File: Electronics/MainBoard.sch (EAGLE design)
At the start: 10 parts, among them J1 1X2-3.5MM

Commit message: nearly done
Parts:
- added R1, R2: (no value), fab:RES-US1206
- added U$1: USB-MINIB-5PIN, SparkFun:USB-MINIB-5PIN
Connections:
- removed net A16: JP1.16
- removed net G_ENC_A_2: JP5.7
- removed net G_ENC_B_2: JP5.8
- removed net P12: JP1.12
- removed net P21: JP2.1
- removed net P22: JP2.2
- removed net P23: JP2.3
- removed net P24: JP2.4
- removed net P25: JP2.5
- removed net P26: JP2.6
- removed net P29: JP2.9
- removed net P30: JP2.10
- new net A_20: JP1.20
- new net D+: JP2.11, R2.1, U$1.D+
- new net D-: JP2.12, R1.1, U$1.D-
- new net G_ENCA_2: JP2.3, JP5.7
- new net G_ENCB_2: JP2.4, JP5.8
- new net P5: JP1.5
- net GND: now also R1.2, R2.2, U$1.GND
- net G_CS_2: now also JP1.16; no longer JP1.20
- net G_DIR_2: now also JP1.12
- net G_PWM_1: now also JP2.2; no longer JP1.5
- net G_PWM_2: now also JP2.1
- net MOT_DIR: now also JP2.5
- net MOT_ENC_A: now also JP2.10
- net MOT_ENC_B: now also JP2.9
- net MOT_PWM: now also JP2.6
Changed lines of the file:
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@@
 <part name="8V1" library="SparkFun" deviceset="VCC" device="" value="8V"/>
 <part name="8V2" library="SparkFun" deviceset="VCC" device="" value="8V"/>
+<part name="R1" library="fab" deviceset="RES-US" device="1206"/>
+<part name="R2" library="fab" deviceset="RES-US" device="1206"/>
+<part name="GND2" library="SparkFun" deviceset="GND" device=""/>
+<part name="U$1" library="SparkFun" deviceset="USB-MINIB" device="-5PIN"/>
+<part name="GND3" library="SparkFun" deviceset="GND" device=""/>
 </parts>
 <sheets>
@@
 <instance part="8V1" gate="1" x="78.74" y="193.04"/>
 <instance part="8V2" gate="1" x="45.72" y="170.18"/>
+<instance part="R1" gate="G$1" x="81.28" y="88.9"/>
+<instance part="R2" gate="G$1" x="81.28" y="83.82"/>
+<instance part="GND2" gate="1" x="91.44" y="78.74"/>
+<instance part="U$1" gate="G$1" x="-15.24" y="137.16"/>
+<instance part="GND3" gate="1" x="-30.48" y="132.08"/>
 </instances>
 <busses>
@@
 <wire x1="-20.32" y1="193.04" x2="-22.86" y2="193.04" width="0.1524" layer="91"/>
 </segment>
+<segment>
+<pinref part="R2" gate="G$1" pin="2"/>
+<wire x1="86.36" y1="83.82" x2="91.44" y2="83.82" width="0.1524" layer="91"/>
+<wire x1="91.44" y1="83.82" x2="91.44" y2="88.9" width="0.1524" layer="91"/>
+<pinref part="R1" gate="G$1" pin="2"/>
+<wire x1="91.44" y1="88.9" x2="86.36" y2="88.9" width="0.1524" layer="91"/>
+<pinref part="GND2" gate="1" pin="GND"/>
+<wire x1="91.44" y1="83.82" x2="91.44" y2="81.28" width="0.1524" layer="91"/>
+<junction x="91.44" y="83.82"/>
+</segment>
+<segment>
+<pinref part="U$1" gate="G$1" pin="GND"/>
+<wire x1="-17.78" y1="137.16" x2="-30.48" y2="137.16" width="0.1524" layer="91"/>
+<pinref part="GND3" gate="1" pin="GND"/>
+<wire x1="-30.48" y1="137.16" x2="-30.48" y2="134.62" width="0.1524" layer="91"/>
+</segment>
 </net>
 <net name="5V" class="0">
@@
 </segment>
 </net>
-<net name="P30" class="0">
-<segment>
-<pinref part="JP2" gate="A" pin="10"/>
-<wire x1="45.72" y1="81.28" x2="73.66" y2="81.28" width="0.1524" layer="91"/>
-<label x="53.34" y="81.28" size="1.778" layer="95"/>
-</segment>
-</net>
-<net name="P29" class="0">
-<segment>
-<pinref part="JP2" gate="A" pin="9"/>
-<wire x1="45.72" y1="78.74" x2="73.66" y2="78.74" width="0.1524" layer="91"/>
-<label x="53.34" y="78.74" size="1.778" layer="95"/>
-</segment>
-</net>
-<net name="P26" class="0">
-<segment>
-<pinref part="JP2" gate="A" pin="6"/>
-<wire x1="45.72" y1="71.12" x2="73.66" y2="71.12" width="0.1524" layer="91"/>
-<label x="53.34" y="71.12" size="1.778" layer="95"/>
-</segment>
-</net>
-<net name="P25" class="0">
-<segment>
-<pinref part="JP2" gate="A" pin="5"/>
-<wire x1="45.72" y1="68.58" x2="73.66" y2="68.58" width="0.1524" layer="91"/>
-<label x="53.34" y="68.58" size="1.778" layer="95"/>
-</segment>
-</net>
-<net name="P24" class="0">
+<net name="G_ENCB_2" class="0">
 <segment>
 <pinref part="JP2" gate="A" pin="4"/>
@@
 <label x="53.34" y="66.04" size="1.778" layer="95"/>
 </segment>
-</net>
-<net name="P22" class="0">
-<segment>
-<pinref part="JP2" gate="A" pin="2"/>
-<wire x1="45.72" y1="60.96" x2="73.66" y2="60.96" width="0.1524" layer="91"/>
-<label x="53.34" y="60.96" size="1.778" layer="95"/>
-</segment>
-</net>
-<net name="P21" class="0">
-<segment>
-<pinref part="JP2" gate="A" pin="1"/>
-<wire x1="45.72" y1="58.42" x2="73.66" y2="58.42" width="0.1524" layer="91"/>
-<label x="53.34" y="58.42" size="1.778" layer="95"/>
-</segment>
-</net>
-<net name="P12" class="0">
-<segment>
-<pinref part="JP1" gate="A" pin="12"/>
-<wire x1="15.24" y1="78.74" x2="-7.62" y2="78.74" width="0.1524" layer="91"/>
-<label x="-7.62" y="78.74" size="1.778" layer="95"/>
+<segment>
+<pinref part="JP5" gate="G$1" pin="8"/>
+<wire x1="68.58" y1="147.32" x2="48.26" y2="147.32" width="0.1524" layer="91"/>
+<label x="48.26" y="147.32" size="1.778" layer="95"/>
 </segment>
 </net>
@@
 <wire x1="15.24" y1="73.66" x2="-7.62" y2="73.66" width="0.1524" layer="91"/>
 <label x="-7.62" y="73.66" size="1.778" layer="95"/>
-</segment>
-</net>
-<net name="A16" class="0">
-<segment>
-<pinref part="JP1" gate="A" pin="16"/>
-<wire x1="15.24" y1="68.58" x2="-7.62" y2="68.58" width="0.1524" layer="91"/>
-<label x="-7.62" y="68.58" size="1.778" layer="95"/>
 </segment>
 </net>
@@
 </segment>
 </net>
-<net name="P23" class="0">
+<net name="G_ENCA_2" class="0">
 <segment>
 <pinref part="JP2" gate="A" pin="3"/>
 <wire x1="45.72" y1="63.5" x2="73.66" y2="63.5" width="0.1524" layer="91"/>
 <label x="53.34" y="63.5" size="1.778" layer="95"/>
+</segment>
+<segment>
+<pinref part="JP5" gate="G$1" pin="7"/>
+<wire x1="68.58" y1="149.86" x2="48.26" y2="149.86" width="0.1524" layer="91"/>
+<label x="48.26" y="149.86" size="1.778" layer="95"/>
 </segment>
 </net>
@@
 </segment>
 <segment>
-<pinref part="JP1" gate="A" pin="5"/>
-<wire x1="15.24" y1="96.52" x2="-7.62" y2="96.52" width="0.1524" layer="91"/>
-<label x="-7.62" y="96.52" size="1.778" layer="95"/>
+<pinref part="JP2" gate="A" pin="2"/>
+<wire x1="45.72" y1="60.96" x2="73.66" y2="60.96" width="0.1524" layer="91"/>
+<label x="53.34" y="60.96" size="1.778" layer="95"/>
 </segment>
 </net>
@@
 <label x="48.26" y="154.94" size="1.778" layer="95"/>
 </segment>
+<segment>
+<pinref part="JP2" gate="A" pin="1"/>
+<wire x1="45.72" y1="58.42" x2="73.66" y2="58.42" width="0.1524" layer="91"/>
+<label x="53.34" y="58.42" size="1.778" layer="95"/>
+</segment>
 </net>
 <net name="G_DIR_2" class="0">
@@
 <label x="48.26" y="152.4" size="1.778" layer="95"/>
 </segment>
-</net>
-<net name="G_ENC_A_2" class="0">
-<segment>
-<pinref part="JP5" gate="G$1" pin="7"/>
-<wire x1="68.58" y1="149.86" x2="48.26" y2="149.86" width="0.1524" layer="91"/>
-<label x="48.26" y="149.86" size="1.778" layer="95"/>
-</segment>
-</net>
-<net name="G_ENC_B_2" class="0">
-<segment>
-<pinref part="JP5" gate="G$1" pin="8"/>
-<wire x1="68.58" y1="147.32" x2="48.26" y2="147.32" width="0.1524" layer="91"/>
-<label x="48.26" y="147.32" size="1.778" layer="95"/>
+<segment>
+<pinref part="JP1" gate="A" pin="12"/>
+<wire x1="15.24" y1="78.74" x2="-7.62" y2="78.74" width="0.1524" layer="91"/>
+<label x="-7.62" y="78.74" size="1.778" layer="95"/>
 </segment>
 </net>
@@
 <label x="17.78" y="149.86" size="1.778" layer="95"/>
 </segment>
+<segment>
+<pinref part="JP2" gate="A" pin="9"/>
+<wire x1="45.72" y1="78.74" x2="73.66" y2="78.74" width="0.1524" layer="91"/>
+<label x="53.34" y="78.74" size="1.778" layer="95"/>
+</segment>
 </net>
 <net name="MOT_PWM" class="0">
@@
 <label x="17.78" y="147.32" size="1.778" layer="95"/>
 </segment>
+<segment>
+<pinref part="JP2" gate="A" pin="6"/>
+<wire x1="45.72" y1="71.12" x2="73.66" y2="71.12" width="0.1524" layer="91"/>
+<label x="53.34" y="71.12" size="1.778" layer="95"/>
+</segment>
 </net>
 <net name="MOT_DIR" class="0">
@@
 <wire x1="38.1" y1="144.78" x2="17.78" y2="144.78" width="0.1524" layer="91"/>
 <label x="17.78" y="144.78" size="1.778" layer="95"/>
+</segment>
+<segment>
+<pinref part="JP2" gate="A" pin="5"/>
+<wire x1="45.72" y1="68.58" x2="73.66" y2="68.58" width="0.1524" layer="91"/>
+<label x="53.34" y="68.58" size="1.778" layer="95"/>
 </segment>
 </net>
@@
 </segment>
 <segment>
-<pinref part="JP1" gate="A" pin="20"/>
-<wire x1="15.24" y1="58.42" x2="-7.62" y2="58.42" width="0.1524" layer="91"/>
-<label x="-7.62" y="58.42" size="1.778" layer="95"/>
+<pinref part="JP1" gate="A" pin="16"/>
+<wire x1="15.24" y1="68.58" x2="-7.62" y2="68.58" width="0.1524" layer="91"/>
+<label x="-7.62" y="68.58" size="1.778" layer="95"/>
 </segment>
 </net>
@@
 <wire x1="38.1" y1="152.4" x2="17.78" y2="152.4" width="0.1524" layer="91"/>
 <label x="17.78" y="152.4" size="1.778" layer="95"/>
+</segment>
+<segment>
+<pinref part="JP2" gate="A" pin="10"/>
+<wire x1="45.72" y1="81.28" x2="73.66" y2="81.28" width="0.1524" layer="91"/>
+<label x="53.34" y="81.28" size="1.778" layer="95"/>
 </segment>
 </net>
@@
 </segment>
 </net>
+<net name="P5" class="0">
+<segment>
+<pinref part="JP1" gate="A" pin="5"/>
+<wire x1="15.24" y1="96.52" x2="-7.62" y2="96.52" width="0.1524" layer="91"/>
+<label x="-7.62" y="96.52" size="1.778" layer="95"/>
+</segment>
+</net>
+<net name="A_20" class="0">
+<segment>
+<pinref part="JP1" gate="A" pin="20"/>
+<wire x1="15.24" y1="58.42" x2="-7.62" y2="58.42" width="0.1524" layer="91"/>
+<label x="-7.62" y="58.42" size="1.778" layer="95"/>
+</segment>
+</net>
+<net name="D+" class="0">
+<segment>
+<pinref part="JP2" gate="A" pin="11"/>
+<wire x1="45.72" y1="83.82" x2="60.96" y2="83.82" width="0.1524" layer="91"/>
+<label x="53.34" y="83.82" size="1.778" layer="95"/>
+<pinref part="R2" gate="G$1" pin="1"/>
+<wire x1="60.96" y1="83.82" x2="76.2" y2="83.82" width="0.1524" layer="91"/>
+</segment>
+<segment>
+<pinref part="U$1" gate="G$1" pin="D+"/>
+<wire x1="-17.78" y1="142.24" x2="-30.48" y2="142.24" width="0.1524" layer="91"/>
+<label x="-27.94" y="142.24" size="1.778" layer="95"/>
+</segment>
+</net>
+<net name="D-" class="0">
+<segment>
+<pinref part="JP2" gate="A" pin="12"/>
+<wire x1="45.72" y1="86.36" x2="60.96" y2="86.36" width="0.1524" layer="91"/>
+<label x="53.34" y="86.36" size="1.778" layer="95"/>
+<wire x1="60.96" y1="86.36" x2="73.66" y2="86.36" width="0.1524" layer="91"/>
+<wire x1="73.66" y1="86.36" x2="73.66" y2="88.9" width="0.1524" layer="91"/>
+<pinref part="R1" gate="G$1" pin="1"/>
+<wire x1="73.66" y1="88.9" x2="76.2" y2="88.9" width="0.1524" layer="91"/>
+</segment>
+<segment>
+<pinref part="U$1" gate="G$1" pin="D-"/>
+<wire x1="-17.78" y1="144.78" x2="-30.48" y2="144.78" width="0.1524" layer="91"/>
+<label x="-27.94" y="144.78" size="1.778" layer="95"/>
+</segment>
+</net>

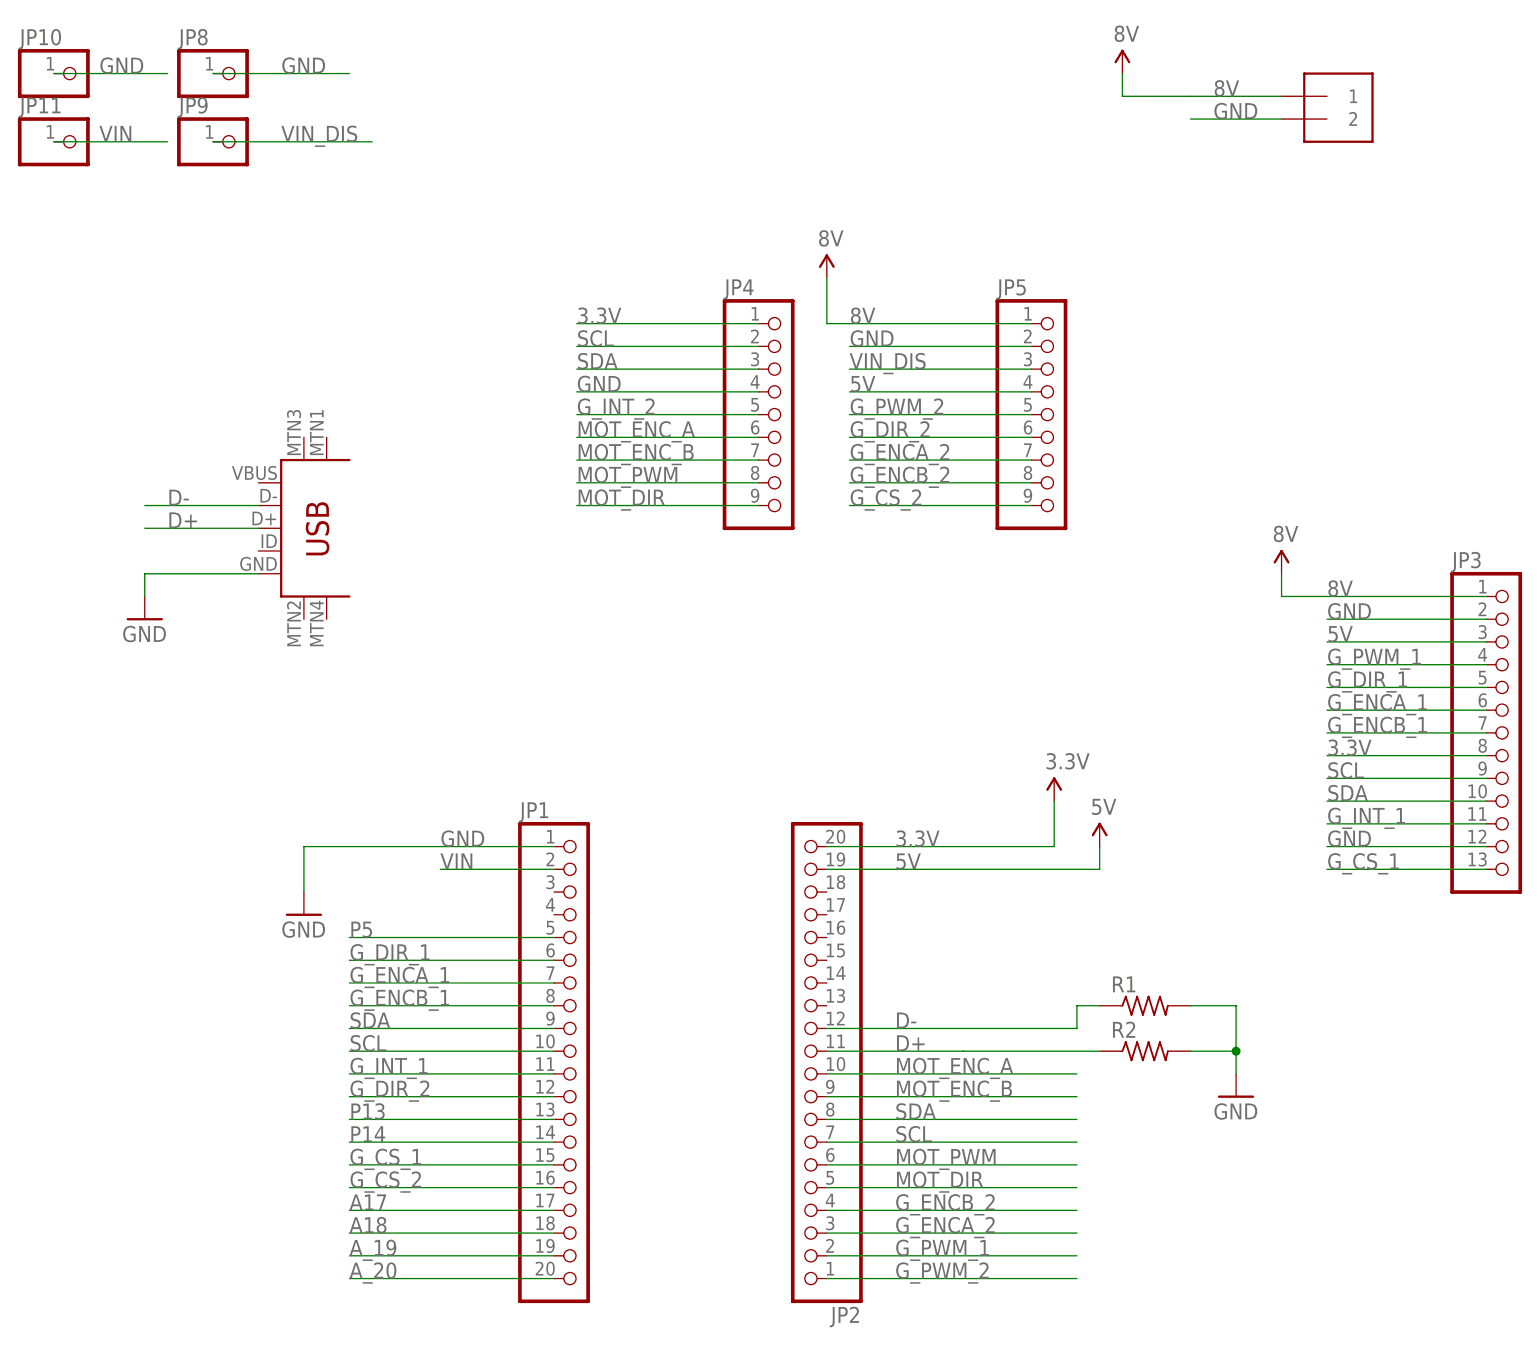
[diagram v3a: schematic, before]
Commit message: main board final layout v1
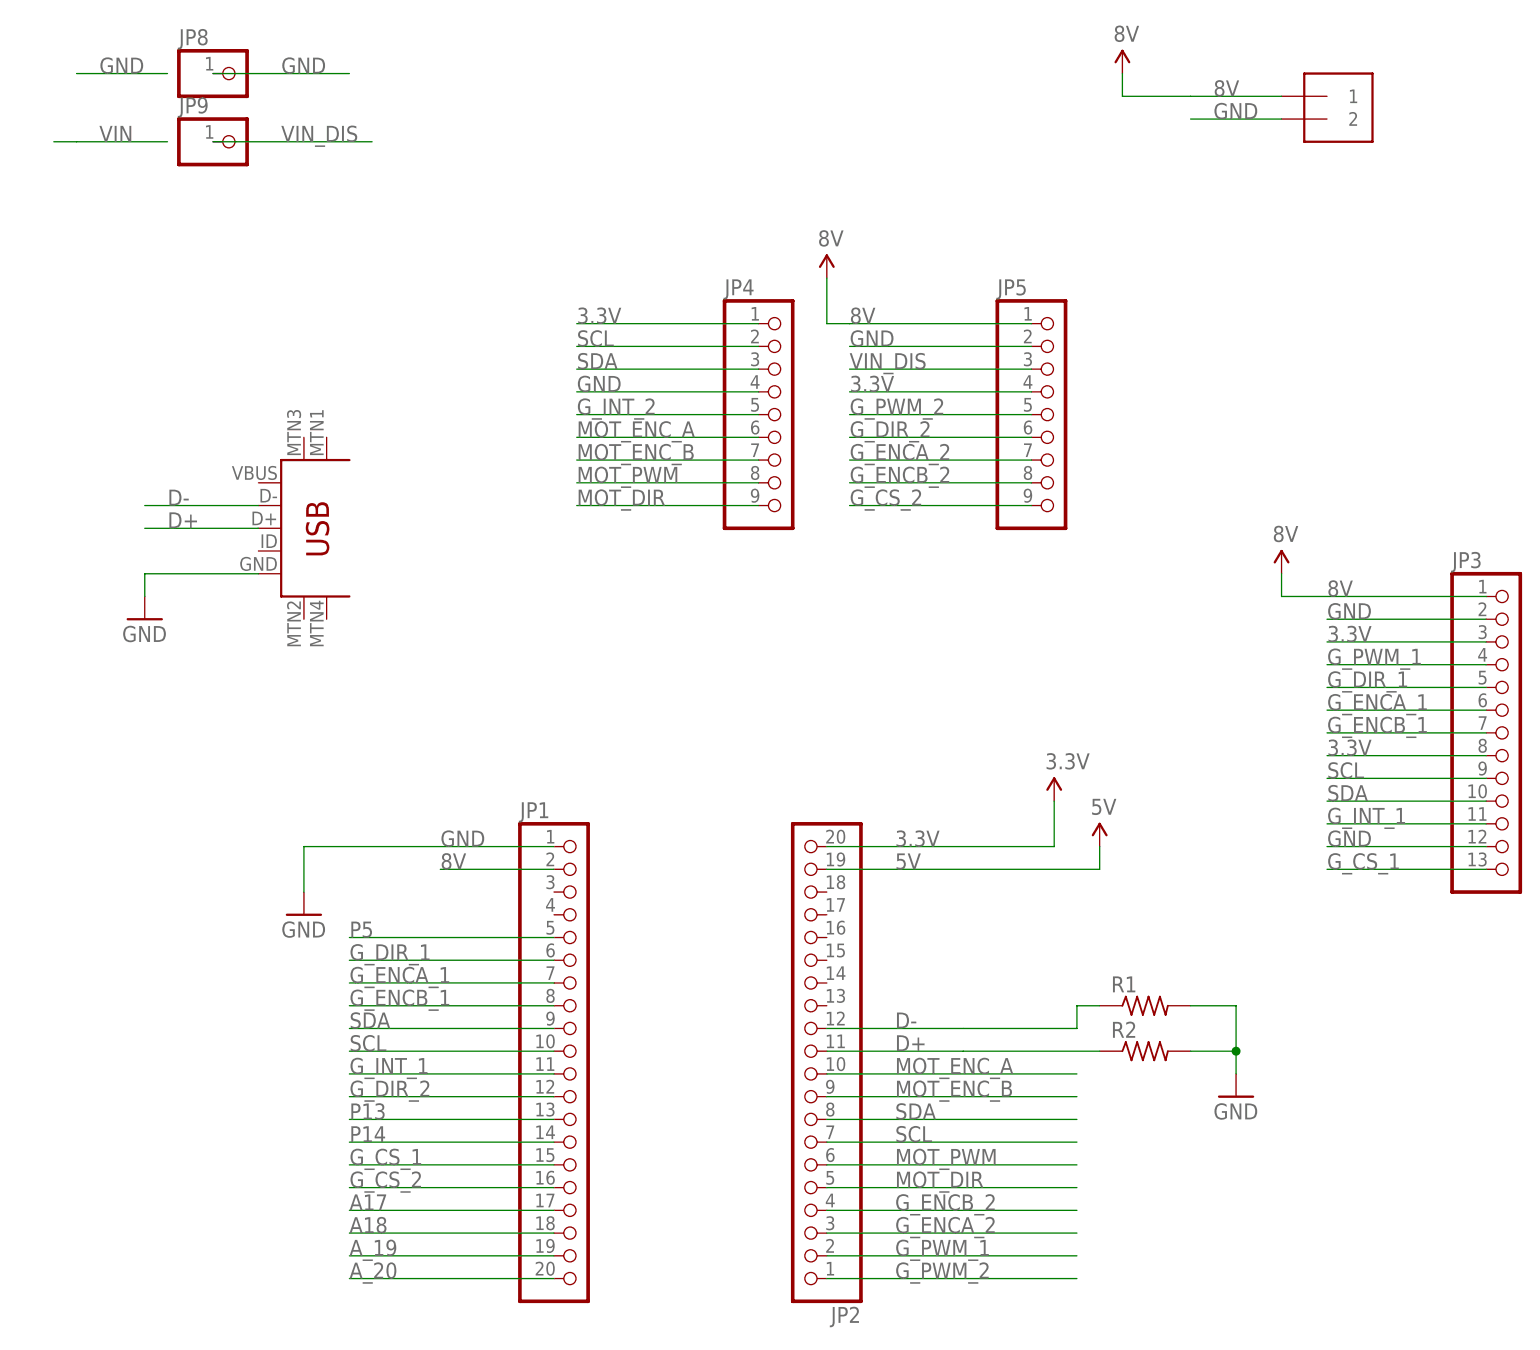
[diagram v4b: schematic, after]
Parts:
- removed JP10, JP11: (no value), adafruit:PINHD-1X1
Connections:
- removed net VIN: JP1.2, JP11.1
- net 3.3V: now also JP3.3, JP5.4
- net 5V: no longer JP3.3, JP5.4
- net 8V: now also JP1.2
- net GND: no longer JP10.1
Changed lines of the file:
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@@
 <part name="JP8" library="adafruit" deviceset="PINHD-1X1" device=""/>
 <part name="JP9" library="adafruit" deviceset="PINHD-1X1" device=""/>
-<part name="JP10" library="adafruit" deviceset="PINHD-1X1" device=""/>
-<part name="JP11" library="adafruit" deviceset="PINHD-1X1" device=""/>
 <part name="J1" library="adafruit" deviceset="1X2" device="-3.5MM"/>
 <part name="8V" library="SparkFun" deviceset="VCC" device="" value="8V"/>
@@
 <instance part="JP8" gate="G$1" x="-20.32" y="193.04"/>
 <instance part="JP9" gate="G$1" x="-20.32" y="185.42"/>
-<instance part="JP10" gate="G$1" x="-38.1" y="193.04"/>
-<instance part="JP11" gate="G$1" x="-38.1" y="185.42"/>
 <instance part="J1" gate="G$1" x="101.6" y="187.96"/>
 <instance part="8V" gate="1" x="96.52" y="137.16"/>
@@
 <wire x1="-38.1" y1="193.04" x2="-27.94" y2="193.04" width="0.1524" layer="91"/>
 <label x="-35.56" y="193.04" size="1.778" layer="95"/>
-<pinref part="JP10" gate="G$1" pin="1"/>
-<wire x1="-38.1" y1="193.04" x2="-40.64" y2="193.04" width="0.1524" layer="91"/>
 </segment>
 <segment>
@@
 <label x="53.34" y="104.14" size="1.778" layer="95"/>
 </segment>
-<segment>
-<pinref part="JP3" gate="A" pin="3"/>
-<wire x1="119.38" y1="129.54" x2="101.6" y2="129.54" width="0.1524" layer="91"/>
-<label x="101.6" y="129.54" size="1.778" layer="95"/>
-</segment>
-<segment>
-<pinref part="JP5" gate="G$1" pin="4"/>
-<wire x1="68.58" y1="157.48" x2="48.26" y2="157.48" width="0.1524" layer="91"/>
-<label x="48.26" y="157.48" size="1.778" layer="95"/>
-</segment>
 </net>
 <net name="SCL" class="0">
@@
 <wire x1="38.1" y1="165.1" x2="17.78" y2="165.1" width="0.1524" layer="91"/>
 <label x="17.78" y="165.1" size="1.778" layer="95"/>
+</segment>
+<segment>
+<pinref part="JP3" gate="A" pin="3"/>
+<wire x1="119.38" y1="129.54" x2="101.6" y2="129.54" width="0.1524" layer="91"/>
+<label x="101.6" y="129.54" size="1.778" layer="95"/>
+</segment>
+<segment>
+<pinref part="JP5" gate="G$1" pin="4"/>
+<wire x1="68.58" y1="157.48" x2="48.26" y2="157.48" width="0.1524" layer="91"/>
+<label x="48.26" y="157.48" size="1.778" layer="95"/>
 </segment>
 </net>
@@
 <wire x1="45.72" y1="165.1" x2="45.72" y2="170.18" width="0.1524" layer="91"/>
 </segment>
+<segment>
+<pinref part="JP1" gate="A" pin="2"/>
+<wire x1="15.24" y1="104.14" x2="2.54" y2="104.14" width="0.1524" layer="91"/>
+<label x="2.54" y="104.14" size="1.778" layer="95"/>
+</segment>
 </net>
 <net name="G_PWM_1" class="0">
@@
 <net name="VIN" class="0">
 <segment>
-<pinref part="JP1" gate="A" pin="2"/>
-<wire x1="15.24" y1="104.14" x2="2.54" y2="104.14" width="0.1524" layer="91"/>
-<label x="2.54" y="104.14" size="1.778" layer="95"/>
-</segment>
-<segment>
 <wire x1="-38.1" y1="185.42" x2="-27.94" y2="185.42" width="0.1524" layer="91"/>
 <label x="-35.56" y="185.42" size="1.778" layer="95"/>
-<pinref part="JP11" gate="G$1" pin="1"/>
 <wire x1="-38.1" y1="185.42" x2="-40.64" y2="185.42" width="0.1524" layer="91"/>
 </segment>

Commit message: mbed code
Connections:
- new net N$1: U$1.VBUS
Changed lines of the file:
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@@
+</segment>
+</net>
+<net name="N$1" class="0">
+<segment>
+<pinref part="U$1" gate="G$1" pin="VBUS"/>
+<wire x1="-17.78" y1="147.32" x2="-30.48" y2="147.32" width="0.1524" layer="91"/>
 </segment>
 </net>
